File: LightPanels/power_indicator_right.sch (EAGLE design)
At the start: 22 parts

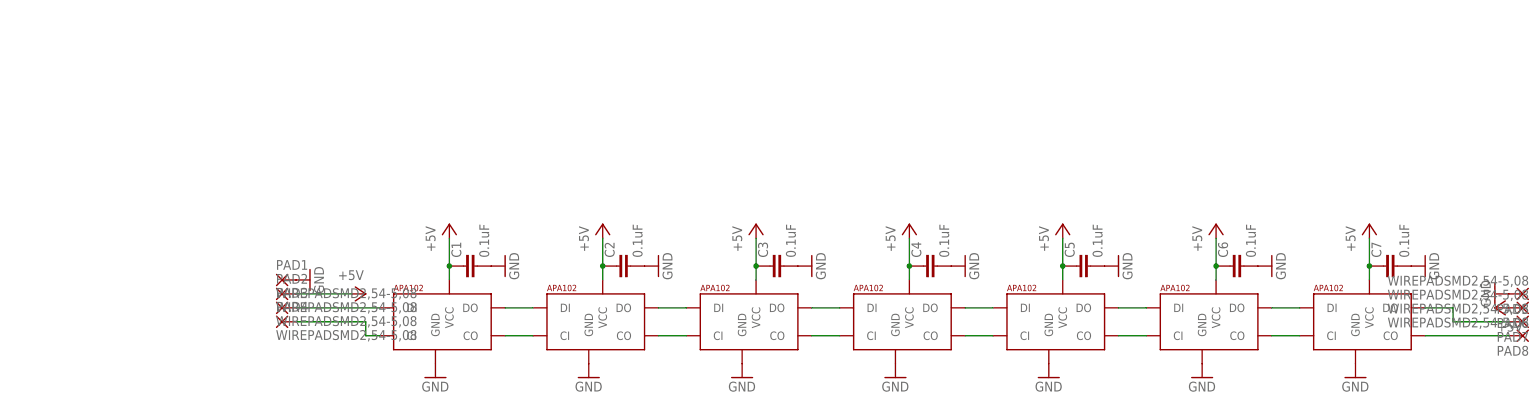
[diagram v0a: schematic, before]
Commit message: Power indicators more or less done
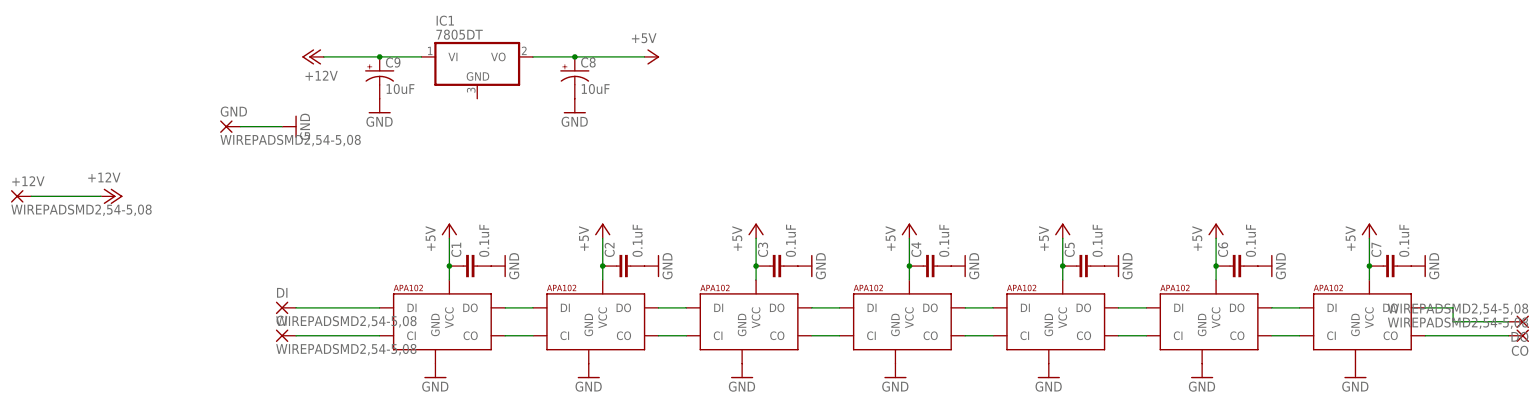
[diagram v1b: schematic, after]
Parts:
- removed PAD1, PAD2, PAD4, PAD5, PAD6: WIREPADSMD2,54-5,08, wirepad:WIREPADSMD2,54-5,08
- added +12V, CI, GND: WIREPADSMD2,54-5,08, wirepad:WIREPADSMD2,54-5,08
- added C8, C9: 10uF, SparkFun-Retired:10UF-TANT
- added IC1: 7805DT, linear:7805DT
- renumbered PAD3 to DI, PAD7 to DO, PAD8 to CO
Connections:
- new net +12V: +12V.P, C9.+, IC1.VI
- net +5V: now also C8.+, IC1.VO; no longer PAD2.P, PAD6.P
- net GND: now also C8.-, C9.-, GND.P; no longer PAD1.P, PAD5.P
- net N$16: now also CI.P; no longer PAD4.P
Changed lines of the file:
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@@
 <part name="P+7" library="supply1" deviceset="+5V" device=""/>
 <part name="P+8" library="supply1" deviceset="+5V" device=""/>
-<part name="P+9" library="supply1" deviceset="+5V" device=""/>
+<part name="GND" library="wirepad" deviceset="WIREPAD" device="SMD2,54-5,08"/>
+<part name="+12V" library="wirepad" deviceset="WIREPAD" device="SMD2,54-5,08"/>
+<part name="DI" library="wirepad" deviceset="WIREPAD" device="SMD2,54-5,08"/>
+<part name="CI" library="wirepad" deviceset="WIREPAD" device="SMD2,54-5,08"/>
+<part name="DO" library="wirepad" deviceset="WIREPAD" device="SMD2,54-5,08"/>
+<part name="CO" library="wirepad" deviceset="WIREPAD" device="SMD2,54-5,08"/>
+<part name="IC1" library="linear" deviceset="78*" device="DT" technology="05"/>
+<part name="P+9" library="supply1" deviceset="+12V" device=""/>
+<part name="P+10" library="supply1" deviceset="+12V" device=""/>
 <part name="GND16" library="supply1" deviceset="GND" device=""/>
-<part name="PAD1" library="wirepad" deviceset="WIREPAD" device="SMD2,54-5,08"/>
-<part name="PAD2" library="wirepad" deviceset="WIREPAD" device="SMD2,54-5,08"/>
-<part name="PAD3" library="wirepad" deviceset="WIREPAD" device="SMD2,54-5,08"/>
-<part name="PAD4" library="wirepad" deviceset="WIREPAD" device="SMD2,54-5,08"/>
-<part name="PAD5" library="wirepad" deviceset="WIREPAD" device="SMD2,54-5,08"/>
-<part name="PAD6" library="wirepad" deviceset="WIREPAD" device="SMD2,54-5,08"/>
-<part name="PAD7" library="wirepad" deviceset="WIREPAD" device="SMD2,54-5,08"/>
-<part name="PAD8" library="wirepad" deviceset="WIREPAD" device="SMD2,54-5,08"/>
+<part name="GND17" library="supply1" deviceset="GND" device=""/>
+<part name="C8" library="SparkFun-Retired" deviceset="10UF-TANT" device="" value="10uF"/>
+<part name="C9" library="SparkFun-Retired" deviceset="10UF-TANT" device="" value="10uF"/>
 </parts>
 <sheets>
@@
 <instance part="C7" gate="G$1" x="187.96" y="91.44" rot="R90"/>
 <instance part="GND14" gate="1" x="193.04" y="91.44" rot="R90"/>
-<instance part="P+5" gate="1" x="0" y="86.36" rot="R270"/>
-<instance part="GND15" gate="1" x="-10.16" y="88.9" rot="R90"/>
+<instance part="P+5" gate="1" x="53.34" y="129.54" rot="R270"/>
+<instance part="GND15" gate="1" x="-12.7" y="116.84" rot="R90"/>
 <instance part="P+6" gate="1" x="127" y="99.06"/>
 <instance part="P+7" gate="1" x="154.94" y="99.06"/>
 <instance part="P+8" gate="1" x="182.88" y="99.06"/>
-<instance part="P+9" gate="1" x="205.74" y="83.82" rot="R90"/>
-<instance part="GND16" gate="1" x="205.74" y="86.36" rot="R270"/>
-<instance part="PAD1" gate="G$1" x="-15.24" y="88.9"/>
-<instance part="PAD2" gate="G$1" x="-15.24" y="86.36"/>
-<instance part="PAD3" gate="G$1" x="-15.24" y="83.82"/>
-<instance part="PAD4" gate="G$1" x="-15.24" y="81.28"/>
-<instance part="PAD5" gate="G$1" x="210.82" y="86.36" rot="R180"/>
-<instance part="PAD6" gate="G$1" x="210.82" y="83.82" rot="R180"/>
-<instance part="PAD7" gate="G$1" x="210.82" y="81.28" rot="R180"/>
-<instance part="PAD8" gate="G$1" x="210.82" y="78.74" rot="R180"/>
+<instance part="GND" gate="G$1" x="-25.4" y="116.84"/>
+<instance part="+12V" gate="G$1" x="-63.5" y="104.14"/>
+<instance part="DI" gate="G$1" x="-15.24" y="83.82"/>
+<instance part="CI" gate="G$1" x="-15.24" y="78.74"/>
+<instance part="DO" gate="G$1" x="210.82" y="81.28" rot="R180"/>
+<instance part="CO" gate="G$1" x="210.82" y="78.74" rot="R180"/>
+<instance part="IC1" gate="A1" x="20.32" y="129.54"/>
+<instance part="P+9" gate="1" x="-45.72" y="104.14" rot="R270"/>
+<instance part="P+10" gate="1" x="-10.16" y="129.54" rot="R90"/>
+<instance part="GND16" gate="1" x="38.1" y="119.38"/>
+<instance part="GND17" gate="1" x="2.54" y="119.38"/>
+<instance part="C8" gate="G$1" x="38.1" y="127"/>
+<instance part="C9" gate="G$1" x="2.54" y="127"/>
 </instances>
 <busses>
@@
 <segment>
 <pinref part="GND15" gate="1" pin="GND"/>
-<pinref part="PAD1" gate="G$1" pin="P"/>
+<pinref part="GND" gate="G$1" pin="P"/>
+<wire x1="-22.86" y1="116.84" x2="-15.24" y2="116.84" width="0.1524" layer="91"/>
 </segment>
 <segment>
 <pinref part="GND16" gate="1" pin="GND"/>
-<pinref part="PAD5" gate="G$1" pin="P"/>
+<pinref part="C8" gate="G$1" pin="-"/>
+</segment>
+<segment>
+<pinref part="C9" gate="G$1" pin="-"/>
+<pinref part="GND17" gate="1" pin="GND"/>
 </segment>
 </net>
@@
 </segment>
 <segment>
+<pinref part="IC1" gate="A1" pin="VO"/>
 <pinref part="P+5" gate="1" pin="+5V"/>
-<wire x1="-2.54" y1="86.36" x2="-12.7" y2="86.36" width="0.1524" layer="91"/>
-<pinref part="PAD2" gate="G$1" pin="P"/>
-</segment>
-<segment>
-<pinref part="P+9" gate="1" pin="+5V"/>
-<pinref part="PAD6" gate="G$1" pin="P"/>
+<wire x1="50.8" y1="129.54" x2="38.1" y2="129.54" width="0.1524" layer="91"/>
+<pinref part="C8" gate="G$1" pin="+"/>
+<wire x1="38.1" y1="129.54" x2="30.48" y2="129.54" width="0.1524" layer="91"/>
+<junction x="38.1" y="129.54"/>
 </segment>
 </net>
@@
 <pinref part="U$7" gate="G$1" pin="CO"/>
 <wire x1="193.04" y1="78.74" x2="208.28" y2="78.74" width="0.1524" layer="91"/>
-<pinref part="PAD8" gate="G$1" pin="P"/>
+<pinref part="CO" gate="G$1" pin="P"/>
 </segment>
 </net>
@@
 <wire x1="208.28" y1="81.28" x2="198.12" y2="81.28" width="0.1524" layer="91"/>
 <wire x1="198.12" y1="81.28" x2="198.12" y2="83.82" width="0.1524" layer="91"/>
-<pinref part="PAD7" gate="G$1" pin="P"/>
+<pinref part="DO" gate="G$1" pin="P"/>
 </segment>
 </net>
@@
 <pinref part="U$1" gate="G$1" pin="DI"/>
 <wire x1="-12.7" y1="83.82" x2="2.54" y2="83.82" width="0.1524" layer="91"/>
-<pinref part="PAD3" gate="G$1" pin="P"/>
+<pinref part="DI" gate="G$1" pin="P"/>
 </segment>
 </net>
@@
 <segment>
 <pinref part="U$1" gate="G$1" pin="CI"/>
-<wire x1="2.54" y1="78.74" x2="0" y2="78.74" width="0.1524" layer="91"/>
-<wire x1="0" y1="78.74" x2="0" y2="81.28" width="0.1524" layer="91"/>
-<wire x1="0" y1="81.28" x2="-12.7" y2="81.28" width="0.1524" layer="91"/>
-<pinref part="PAD4" gate="G$1" pin="P"/>
-</segment>
-</net>
+<wire x1="2.54" y1="78.74" x2="-12.7" y2="78.74" width="0.1524" layer="91"/>
+<pinref part="CI" gate="G$1" pin="P"/>
+</segment>
+</net>
+<net name="+12V" class="0">
+<segment>
+<pinref part="P+9" gate="1" pin="+12V"/>
+<pinref part="+12V" gate="G$1" pin="P"/>
+<wire x1="-60.96" y1="104.14" x2="-48.26" y2="104.14" width="0.1524" layer="91"/>
+</segment>
+<segment>
+<pinref part="IC1" gate="A1" pin="VI"/>
+<pinref part="P+10" gate="1" pin="+12V"/>
+<wire x1="-7.62" y1="129.54" x2="2.54" y2="129.54" width="0.1524" layer="91"/>
+<pinref part="C9" gate="G$1" pin="+"/>
+<wire x1="2.54" y1="129.54" x2="10.16" y2="129.54" width="0.1524" layer="91"/>
+<junction x="2.54" y="129.54"/>
+</segment>
+</net>
